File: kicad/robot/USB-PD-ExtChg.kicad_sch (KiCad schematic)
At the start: 28 parts, among them J1 USBC_Receptacle_SMD_RA, Q3 YJL3416A, Q4 YJL3416A, U18 AP33771DKZ-13

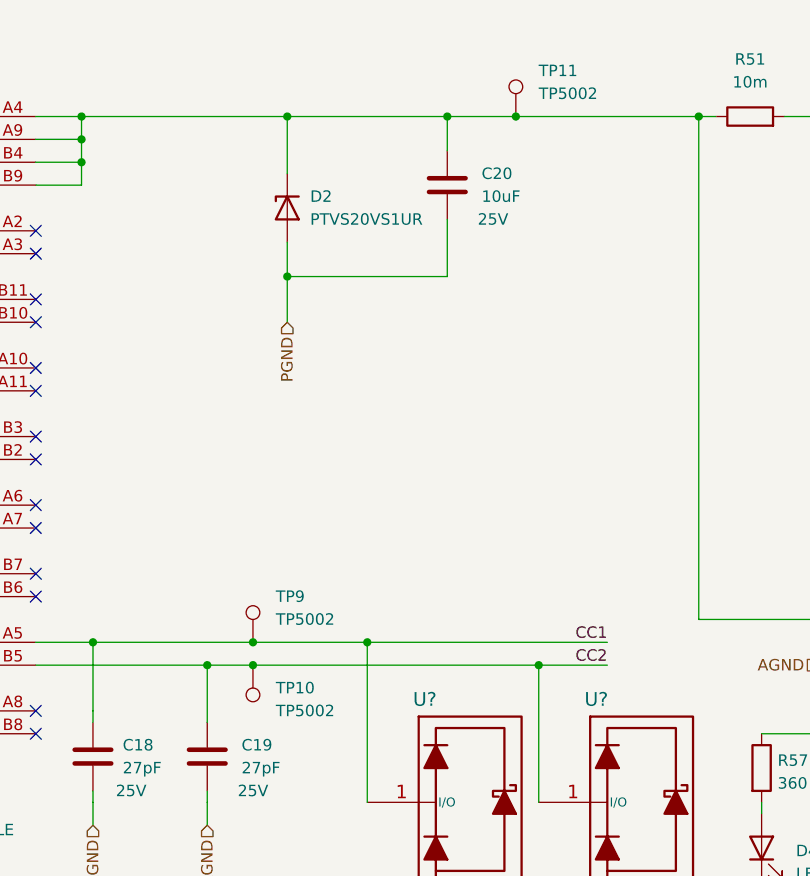
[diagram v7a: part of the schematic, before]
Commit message: Updated Vbus ESD
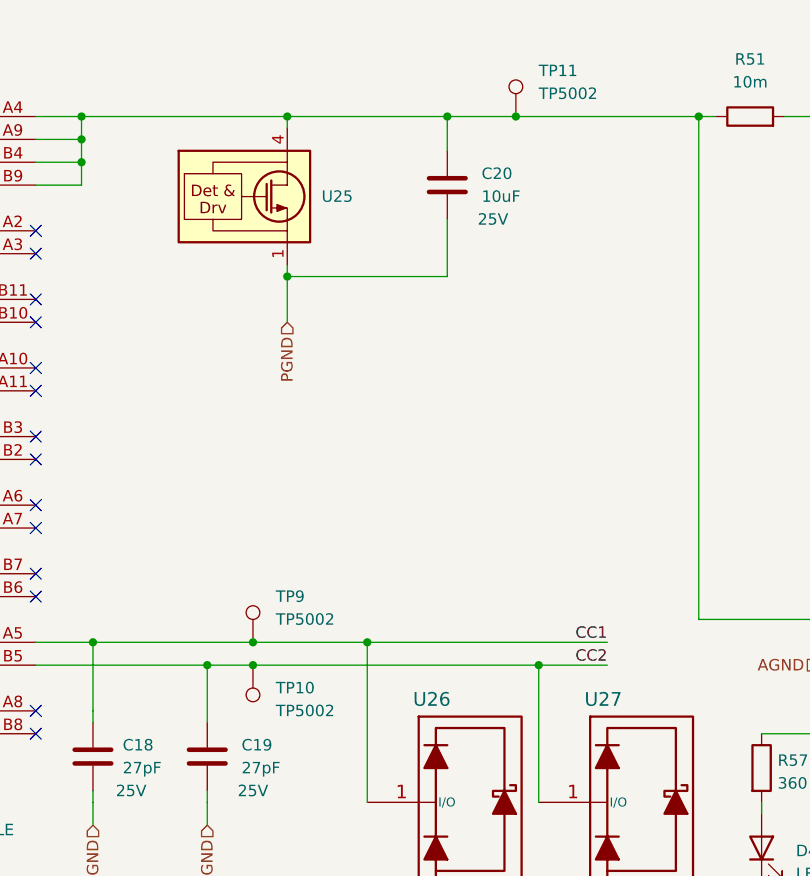
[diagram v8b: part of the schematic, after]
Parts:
- removed D2: PTVS20VS1UR, Diode_SMD:Nexperia_CFP3_SOD-123W, symbol Device:D_Zener
- added U25: TVS0500DRV, Package_SON:TVS0500DRVR, symbol Power_Protection:TVS0500DRV
- gave numbers to parts that had none: 2
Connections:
- net at C20.1, J1.A4 (VBUS), J1.A9 (VBUS)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: now also U25.4 (IN), U25.5 (IN), U25.6 (IN)
- net PGND renamed GND
- net GND: now also U25.1 (GND), U25.2 (GND), U25.3 (GND), U25.7 (GND)
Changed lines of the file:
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@@
   (junction (at 152.4 186.69) (diameter 0) (color 0 0 0 0)
   )
+  (junction (at 207.01 186.69) (diameter 0) (color 0 0 0 0)
+  )
+  (junction (at 210.82 125.73) (diameter 0) (color 0 0 0 0)
+  )
+  (junction (at 207.01 184.15) (diameter 0) (color 0 0 0 0)
+  )
+  (junction (at 152.4 189.23) (diameter 0) (color 0 0 0 0)
+  )
+  (junction (at 307.34 125.73) (diameter 0) (color 0 0 0 0)
+  )
+  (junction (at 152.4 184.15) (diameter 0) (color 0 0 0 0)
+  )
   (junction (at 210.82 143.51) (diameter 0) (color 0 0 0 0)
-  )
-  (junction (at 210.82 125.73) (diameter 0) (color 0 0 0 0)
-  )
-  (junction (at 207.01 186.69) (diameter 0) (color 0 0 0 0)
-  )
-  (junction (at 207.01 184.15) (diameter 0) (color 0 0 0 0)
-  )
-  (junction (at 152.4 189.23) (diameter 0) (color 0 0 0 0)
-  )
-  (junction (at 307.34 125.73) (diameter 0) (color 0 0 0 0)
-  )
-  (junction (at 152.4 184.15) (diameter 0) (color 0 0 0 0)
   )
   (junction (at 337.185 184.15) (diameter 0) (color 0 0 0 0)
@@
   (no_connect (at 182.88 138.43))
   (no_connect (at 182.88 146.05))
+  (wire (pts (xy 210.82 125.73) (xy 228.6 125.73))
+    (stroke (width 0) (type default) (color 0 0 0 0))
+  )
   (wire (pts (xy 284.48 167.64) (xy 284.48 169.545))
     (stroke (width 0) (type default) (color 0 0 0 0))
@@
     (stroke (width 0) (type default) (color 0 0 0 0))
   )
-  (wire (pts (xy 210.82 125.73) (xy 210.82 132.08))
-    (stroke (width 0) (type default) (color 0 0 0 0))
-  )
   (wire (pts (xy 346.075 186.69) (xy 346.075 189.23))
     (stroke (width 0) (type default) (color 0 0 0 0))
@@
     (stroke (width 0) (type default) (color 0 0 0 0))
   )
+  (wire (pts (xy 307.34 133.35) (xy 307.34 148.59))
+    (stroke (width 0) (type default) (color 0 0 0 0))
+  )
+  (wire (pts (xy 228.6 125.73) (xy 236.22 125.73))
+    (stroke (width 0) (type default) (color 0 0 0 0))
+  )
+  (wire (pts (xy 152.4 191.77) (xy 152.4 219.71))
+    (stroke (width 0.254) (type default) (color 0 0 0 0))
+  )
+  (wire (pts (xy 238.76 186.69) (xy 238.76 201.93))
+    (stroke (width 0) (type default) (color 0 0 0 0))
+  )
+  (wire (pts (xy 285.75 209.55) (xy 285.75 207.01))
+    (stroke (width 0) (type default) (color 0 0 0 0))
+  )
+  (wire (pts (xy 297.18 169.545) (xy 297.18 163.83))
+    (stroke (width 0) (type default) (color 0 0 0 0))
+  )
+  (wire (pts (xy 201.93 186.69) (xy 201.93 193.04))
+    (stroke (width 0) (type default) (color 0 0 0 0))
+  )
+  (wire (pts (xy 263.525 201.93) (xy 263.525 203.2))
+    (stroke (width 0) (type default) (color 0 0 0 0))
+  )
+  (wire (pts (xy 300.99 125.73) (xy 307.34 125.73))
+    (stroke (width 0) (type default) (color 0 0 0 0))
+  )
+  (wire (pts (xy 256.54 125.73) (xy 258.445 125.73))
+    (stroke (width 0) (type default) (color 0 0 0 0))
+  )
+  (wire (pts (xy 154.94 184.15) (xy 152.4 184.15))
+    (stroke (width 0.254) (type default) (color 0 0 0 0))
+  )
+  (wire (pts (xy 307.34 133.35) (xy 318.77 133.35))
+    (stroke (width 0) (type default) (color 0 0 0 0))
+  )
+  (wire (pts (xy 328.93 160.02) (xy 328.93 125.73))
+    (stroke (width 0) (type default) (color 0 0 0 0))
+  )
+  (wire (pts (xy 207.01 186.69) (xy 238.76 186.69))
+    (stroke (width 0) (type default) (color 0 0 0 0))
+  )
+  (wire (pts (xy 336.55 135.255) (xy 336.55 137.795))
+    (stroke (width 0) (type default) (color 0 0 0 0))
+  )
+  (wire (pts (xy 210.82 142.24) (xy 210.82 143.51))
+    (stroke (width 0) (type default) (color 0 0 0 0))
+  )
+  (wire (pts (xy 309.245 189.23) (xy 323.215 189.23))
+    (stroke (width 0) (type default) (color 0 0 0 0))
+  )
+  (wire (pts (xy 182.88 184.15) (xy 189.23 184.15))
+    (stroke (width 0.254) (type default) (color 0 0 0 0))
+  )
+  (wire (pts (xy 295.91 233.68) (xy 295.91 207.01))
+    (stroke (width 0) (type default) (color 0 0 0 0))
+  )
+  (wire (pts (xy 189.23 191.77) (xy 189.23 193.04))
+    (stroke (width 0) (type default) (color 0 0 0 0))
+  )
+  (wire (pts (xy 337.185 184.15) (xy 309.245 184.15))
+    (stroke (width 0) (type default) (color 0 0 0 0))
+  )
   (wire (pts (xy 187.96 125.73) (xy 210.82 125.73))
-    (stroke (width 0.254) (type default) (color 0 0 0 0))
-  )
-  (wire (pts (xy 307.34 133.35) (xy 307.34 148.59))
-    (stroke (width 0) (type default) (color 0 0 0 0))
-  )
-  (wire (pts (xy 228.6 125.73) (xy 236.22 125.73))
-    (stroke (width 0) (type default) (color 0 0 0 0))
-  )
-  (wire (pts (xy 152.4 191.77) (xy 152.4 219.71))
-    (stroke (width 0.254) (type default) (color 0 0 0 0))
-  )
-  (wire (pts (xy 238.76 186.69) (xy 238.76 201.93))
-    (stroke (width 0) (type default) (color 0 0 0 0))
-  )
-  (wire (pts (xy 285.75 209.55) (xy 285.75 207.01))
-    (stroke (width 0) (type default) (color 0 0 0 0))
-  )
-  (wire (pts (xy 297.18 169.545) (xy 297.18 163.83))
-    (stroke (width 0) (type default) (color 0 0 0 0))
-  )
-  (wire (pts (xy 201.93 186.69) (xy 201.93 193.04))
-    (stroke (width 0) (type default) (color 0 0 0 0))
-  )
-  (wire (pts (xy 263.525 201.93) (xy 263.525 203.2))
-    (stroke (width 0) (type default) (color 0 0 0 0))
-  )
-  (wire (pts (xy 300.99 125.73) (xy 307.34 125.73))
-    (stroke (width 0) (type default) (color 0 0 0 0))
-  )
-  (wire (pts (xy 256.54 125.73) (xy 258.445 125.73))
-    (stroke (width 0) (type default) (color 0 0 0 0))
-  )
-  (wire (pts (xy 154.94 184.15) (xy 152.4 184.15))
-    (stroke (width 0.254) (type default) (color 0 0 0 0))
-  )
-  (wire (pts (xy 307.34 133.35) (xy 318.77 133.35))
-    (stroke (width 0) (type default) (color 0 0 0 0))
-  )
-  (wire (pts (xy 328.93 160.02) (xy 328.93 125.73))
-    (stroke (width 0) (type default) (color 0 0 0 0))
-  )
-  (wire (pts (xy 207.01 186.69) (xy 238.76 186.69))
-    (stroke (width 0) (type default) (color 0 0 0 0))
-  )
-  (wire (pts (xy 336.55 135.255) (xy 336.55 137.795))
-    (stroke (width 0) (type default) (color 0 0 0 0))
-  )
-  (wire (pts (xy 309.245 189.23) (xy 323.215 189.23))
-    (stroke (width 0) (type default) (color 0 0 0 0))
-  )
-  (wire (pts (xy 182.88 184.15) (xy 189.23 184.15))
-    (stroke (width 0.254) (type default) (color 0 0 0 0))
-  )
-  (wire (pts (xy 295.91 233.68) (xy 295.91 207.01))
-    (stroke (width 0) (type default) (color 0 0 0 0))
-  )
-  (wire (pts (xy 189.23 191.77) (xy 189.23 193.04))
-    (stroke (width 0) (type default) (color 0 0 0 0))
-  )
-  (wire (pts (xy 337.185 184.15) (xy 309.245 184.15))
-    (stroke (width 0) (type default) (color 0 0 0 0))
-  )
-  (wire (pts (xy 210.82 125.73) (xy 228.6 125.73))
     (stroke (width 0) (type default) (color 0 0 0 0))
   )
@@
     (stroke (width 0) (type default) (color 0 0 0 0))
   )
-  (wire (pts (xy 210.82 139.7) (xy 210.82 143.51))
-    (stroke (width 0) (type default) (color 0 0 0 0))
-  )
   (wire (pts (xy 182.88 128.27) (xy 187.96 128.27))
     (stroke (width 0.254) (type default) (color 0 0 0 0))
@@
   )
   (wire (pts (xy 337.185 184.15) (xy 337.185 189.23))
+    (stroke (width 0) (type default) (color 0 0 0 0))
+  )
+  (wire (pts (xy 210.82 125.73) (xy 210.82 127))
     (stroke (width 0) (type default) (color 0 0 0 0))
   )
@@
   (symbol (lib_id "Diode:TPD1E05U06") (at 231.14 201.93 0) (unit 1)
     (in_bom yes) (on_board yes)
-    (property "Reference" "U?" (id 0) (at 224.79 190.5 0)
+    (property "Reference" "U26" (id 0) (at 224.79 190.5 0)
       (effects (font (size 1.524 1.524)) (justify left))
     )
@@
   (symbol (lib_id "Diode:TPD1E05U06") (at 250.19 201.93 0) (unit 1)
     (in_bom yes) (on_board yes)
-    (property "Reference" "U?" (id 0) (at 243.84 190.5 0)
+    (property "Reference" "U27" (id 0) (at 243.84 190.5 0)
       (effects (font (size 1.524 1.524)) (justify left))
     )
@@
     (pin "2")
   )
-  (symbol (lib_id "Device:D_Zener") (at 210.82 135.89 90) (mirror x) (unit 1)
-    (in_bom yes) (on_board yes)
-    (property "Reference" "D2" (id 0) (at 213.36 134.6199 90)
-      (effects (font (size 1.27 1.27)) (justify right))
-    )
-    (property "Value" "PTVS20VS1UR" (id 1) (at 213.36 137.1599 90)
-      (effects (font (size 1.27 1.27)) (justify right))
-    )
-    (property "Footprint" "Diode_SMD:Nexperia_CFP3_SOD-123W" (id 2) (at 210.82 135.89 0)
-      (effects (font (size 1.27 1.27)) hide)
-    )
-    (property "Datasheet" "https://www.mouser.jp/datasheet/2/916/PTVSXS1UR_SER-1545507.pdf" (id 3) (at 210.82 135.89 0)
-      (effects (font (size 1.27 1.27)) hide)
-    )
-    (property "Part Number" "PTVS20VS1UR" (id 4) (at 210.82 135.89 0)
-      (effects (font (size 1.27 1.27)) hide)
-    )
-    (property "Description" "TVS Diode 20V" (id 5) (at 210.82 135.89 0)
-      (effects (font (size 1.27 1.27)) hide)
-    )
-    (property "Manufacturer" "Nexperia" (id 6) (at 210.82 135.89 0)
-      (effects (font (size 1.27 1.27)) hide)
-    )
-    (pin "1")
-    (pin "2")
-  )
   (symbol (lib_id "Device:C") (at 316.865 169.545 0) (unit 1)
     (in_bom yes) (on_board yes)
@@
     (pin "2")
   )
+  (symbol (lib_id "Power_Protection:TVS0500DRV") (at 210.82 134.62 0) (unit 1)
+    (in_bom yes) (on_board yes) (fields_autoplaced)
+    (property "Reference" "U25" (id 0) (at 214.63 134.6199 0)
+      (effects (font (size 1.27 1.27)) (justify left))
+    )
+    (property "Value" "TVS0500DRV" (id 1) (at 227.965 132.08 0)
+      (effects (font (size 1.27 1.27)) (justify left) hide)
+    )
+    (property "Footprint" "Package_SON:TVS0500DRVR" (id 2) (at 234.315 133.985 0)
+      (effects (font (size 1.27 1.27)) hide)
+    )
+    (property "Datasheet" "https://www.ti.com/lit/gpn/tvs0500" (id 3) (at 233.68 135.89 0)
+      (effects (font (size 1.27 1.27)) hide)
+    )
+    (pin "1")
+    (pin "2")
+    (pin "3")
+    (pin "4")
+    (pin "5")
+    (pin "6")
+    (pin "7")
+  )
   (symbol (lib_id "Transistor_FET:YJL3416A") (at 318.77 128.27 270) (mirror x) (unit 1)
